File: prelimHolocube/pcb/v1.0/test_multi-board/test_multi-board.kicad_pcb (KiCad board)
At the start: 2 copper layers, 120 x 100 mm, 48 parts

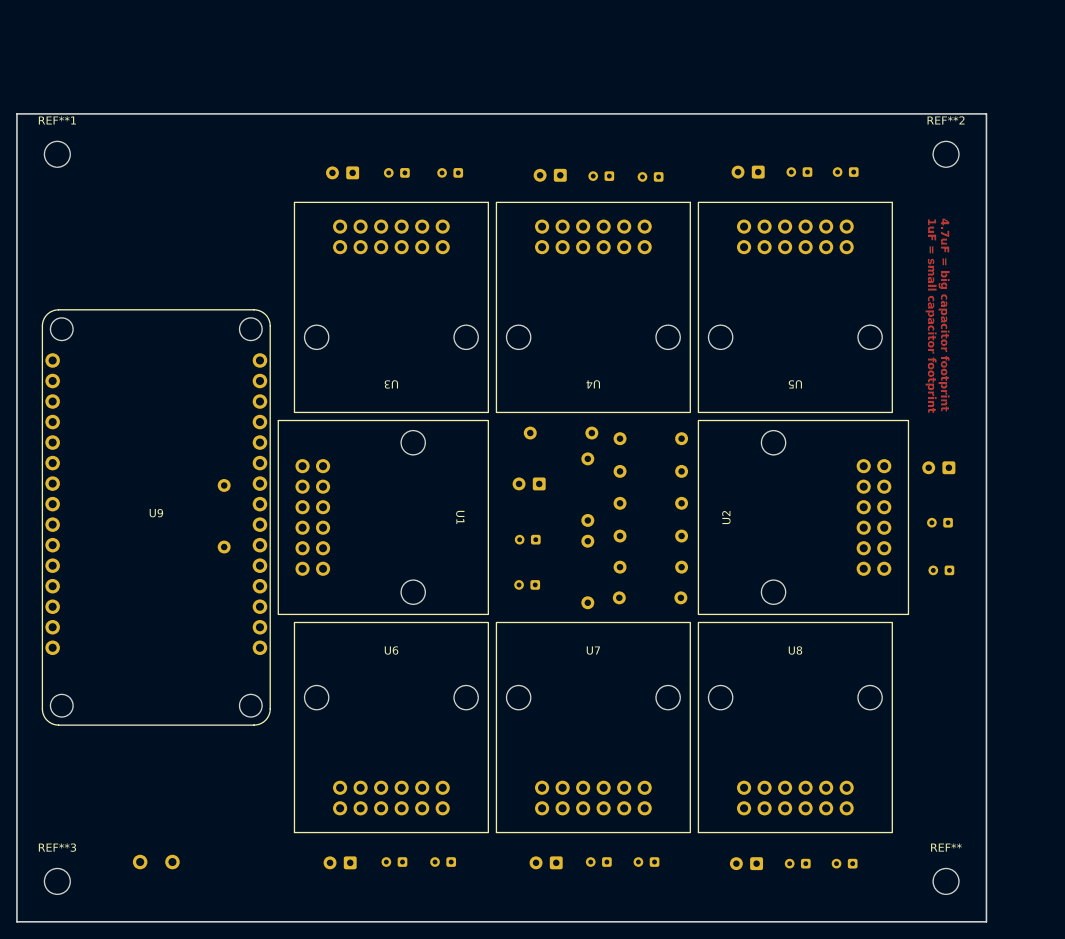
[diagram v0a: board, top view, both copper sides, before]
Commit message: Finish schematic
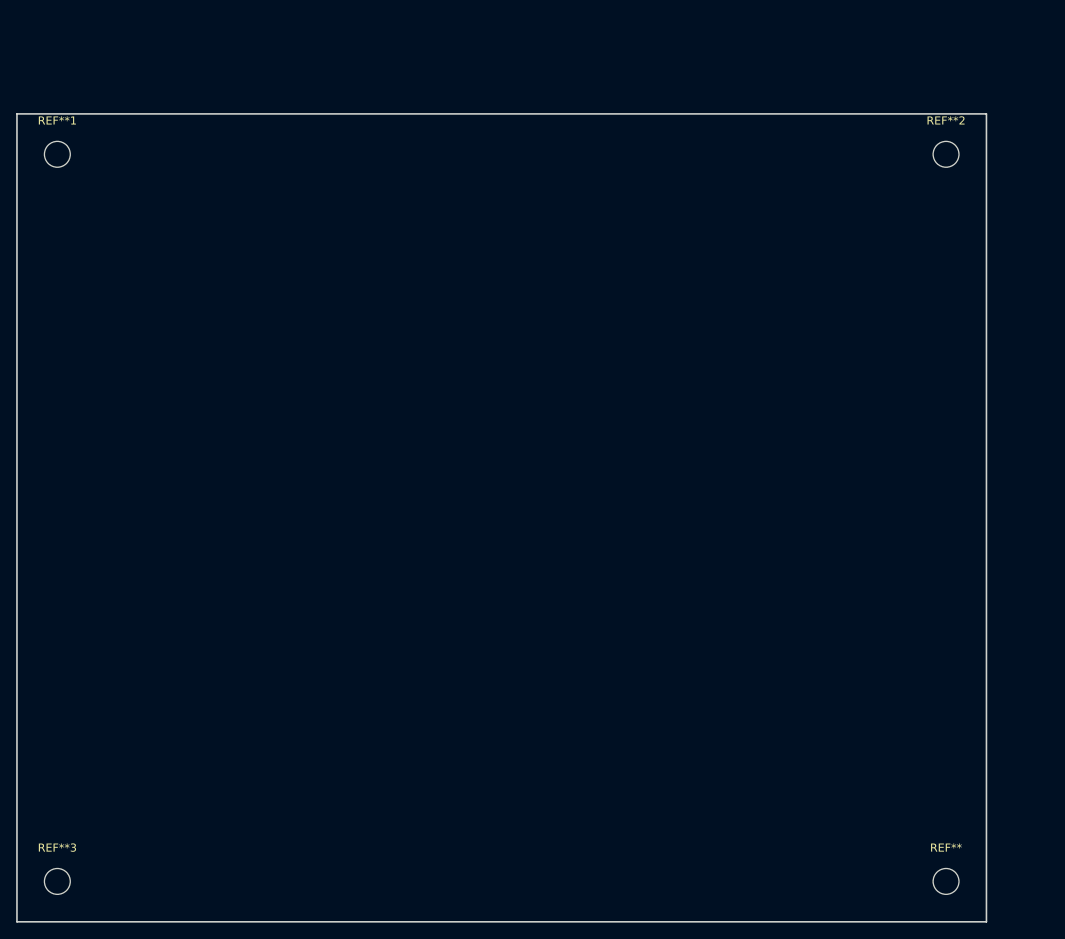
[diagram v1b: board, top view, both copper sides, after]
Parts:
- removed C1, C11, C12, C14, C16, C17, C18, C20, C22, C23, C24, C3, C5, C6, C8, C9: 4.7uF, Capacitor_THT:CP_Radial_D4.0mm_P2.00mm
- removed C10, C13, C15, C19, C2, C21, C4, C7: 1uF ceramic, Capacitor_THT:CP_Radial_D5.0mm_P2.50mm
- removed R1, R10, R2, R4, R5, R6, R7, R8, R9: 1M, Resistor_THT:R_Axial_DIN0207_L6.3mm_D2.5mm_P7.62mm_Horizontal
- removed R3: 10k, Resistor_THT:R_Axial_DIN0207_L6.3mm_D2.5mm_P7.62mm_Horizontal
- removed U1, U2, U3, U4, U5, U6, U7, U8: ~, transparent_oled_display:surenoo-1.12in-128x128
- removed U10: ~, Power_Supply:DC_2-Terminals
- removed U9: ~, esp32:devkitv1-30pin
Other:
- board text removed: "4.7uF = big capacitor footprint 1uF = small capacitor footprint"

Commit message: Finish multiboard pcb
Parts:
- removed REF**: MountingHole_3.2mm_M3, MountingHole:MountingHole_3.2mm_M3
- added C1: 4.7uF, Capacitor_THT:CP_Radial_D4.0mm_P2.00mm, F.Cu at (109.9, 69.6)
- added C10: 4.7uF, Capacitor_THT:CP_Radial_D4.0mm_P2.00mm, F.Cu at (190.6, 69.7)
- added C11: 1uF ceramic, Capacitor_THT:C_Disc_D6.0mm_W2.5mm_P5.00mm, F.Cu at (198.7, 74.5)
- added C12: 4.7uF, Capacitor_THT:CP_Radial_D4.0mm_P2.00mm, F.Cu at (185.3, 69.7)
- added C13: 4.7uF, Capacitor_THT:CP_Radial_D4.0mm_P2.00mm, F.Cu at (119.1, 122.2)
- added C14: 1uF ceramic, Capacitor_THT:C_Disc_D6.0mm_W2.5mm_P5.00mm, F.Cu at (110.8, 117.2)
- added C15: 4.7uF, Capacitor_THT:CP_Radial_D4.0mm_P2.00mm, F.Cu at (124.1, 122.1)
- added C16: 4.7uF, Capacitor_THT:CP_Radial_D4.0mm_P2.00mm, F.Cu at (145.9, 122.1)
- added C17: 1uF ceramic, Capacitor_THT:C_Disc_D6.0mm_W2.5mm_P5.00mm, F.Cu at (137.8, 117.1)
- added C18: 4.7uF, Capacitor_THT:CP_Radial_D4.0mm_P2.00mm, F.Cu at (151.3, 122.0)
- added C19: 4.7uF, Capacitor_THT:CP_Radial_D4.0mm_P2.00mm, F.Cu at (173.2, 121.9)
- added C2: 1uF ceramic, Capacitor_THT:C_Disc_D6.0mm_W2.5mm_P5.00mm, F.Cu at (117.7, 74.5)
- added C20: 1uF ceramic, Capacitor_THT:C_Disc_D6.0mm_W2.5mm_P5.00mm, F.Cu at (165.3, 117.1)
- added C21: 4.7uF, Capacitor_THT:CP_Radial_D4.0mm_P2.00mm, F.Cu at (178.3, 121.9)
- added C22: 4.7uF, Capacitor_THT:CP_Radial_D4.0mm_P2.00mm, F.Cu at (199.5, 121.9)
- added C23: 1uF ceramic, Capacitor_THT:C_Disc_D6.0mm_W2.5mm_P5.00mm, F.Cu at (191.5, 117.1)
- added C24: 4.7uF, Capacitor_THT:CP_Radial_D4.0mm_P2.00mm, F.Cu at (204.8, 121.8)
- added C3: 4.7uF, Capacitor_THT:CP_Radial_D4.0mm_P2.00mm, F.Cu at (104.7, 69.7)
- added C4: 4.7uF, Capacitor_THT:CP_Radial_D4.0mm_P2.00mm, F.Cu at (136.8, 69.6)
- added C5: 1uF ceramic, Capacitor_THT:C_Disc_D6.0mm_W2.5mm_P5.00mm, F.Cu at (144.6, 74.5)
- added C6: 4.7uF, Capacitor_THT:CP_Radial_D4.0mm_P2.00mm, F.Cu at (131.7, 69.6)
- added C7: 4.7uF, Capacitor_THT:CP_Radial_D4.0mm_P2.00mm, F.Cu at (164.0, 69.7)
- added C8: 1uF ceramic, Capacitor_THT:C_Disc_D6.0mm_W2.5mm_P5.00mm, F.Cu at (171.8, 74.6)
- added C9: 4.7uF, Capacitor_THT:CP_Radial_D4.0mm_P2.00mm, F.Cu at (158.7, 69.7)
- added J1: Breakout_1, Connector_PinHeader_2.54mm:PinHeader_1x04_P2.54mm_Vertical, F.Cu at (124.4, 77.8)
- added J2: Breakout_2, Connector_PinHeader_2.54mm:PinHeader_1x04_P2.54mm_Vertical, F.Cu at (151.6, 77.8)
- added J3: Breakout_3, Connector_PinHeader_2.54mm:PinHeader_1x04_P2.54mm_Vertical, F.Cu at (178.7, 77.8)
- added J4: Breakout_4, Connector_PinHeader_2.54mm:PinHeader_1x04_P2.54mm_Vertical, F.Cu at (205.3, 77.8)
- added J5: Breakout_5, Connector_PinHeader_2.54mm:PinHeader_1x04_P2.54mm_Vertical, F.Cu at (104.1, 114.0)
- added J6: Breakout_6, Connector_PinHeader_2.54mm:PinHeader_1x04_P2.54mm_Vertical, F.Cu at (131.1, 113.8)
- added J7: Breakout_7, Connector_PinHeader_2.54mm:PinHeader_1x04_P2.54mm_Vertical, F.Cu at (158.2, 113.7)
- added J8: Breakout_8, Connector_PinHeader_2.54mm:PinHeader_1x04_P2.54mm_Vertical, F.Cu at (184.8, 113.7)
- added R1: 750k, Resistor_THT:R_Axial_DIN0207_L6.3mm_D2.5mm_P7.62mm_Horizontal, F.Cu at (114.2, 77.1)
- added R10: 750k, Resistor_THT:R_Axial_DIN0207_L6.3mm_D2.5mm_P7.62mm_Horizontal, F.Cu at (194.9, 77.1)
- added R11: 10k, Resistor_THT:R_Axial_DIN0207_L6.3mm_D2.5mm_P7.62mm_Horizontal, F.Cu at (151.1, 105.3)
- added R12: 10k, Resistor_THT:R_Axial_DIN0207_L6.3mm_D2.5mm_P7.62mm_Horizontal, F.Cu at (147.8, 105.3)
- added R13: 750k, Resistor_THT:R_Axial_DIN0207_L6.3mm_D2.5mm_P7.62mm_Horizontal, F.Cu at (114.5, 114.6)
- added R14: 10k, Resistor_THT:R_Axial_DIN0207_L6.3mm_D2.5mm_P7.62mm_Horizontal, F.Cu at (162.5, 88.9)
- added R16: 750k, Resistor_THT:R_Axial_DIN0207_L6.3mm_D2.5mm_P7.62mm_Horizontal, F.Cu at (141.4, 114.5)
- added R19: 750k, Resistor_THT:R_Axial_DIN0207_L6.3mm_D2.5mm_P7.62mm_Horizontal, F.Cu at (168.9, 114.5)
- added R2: 10k, Resistor_THT:R_Axial_DIN0207_L6.3mm_D2.5mm_P7.62mm_Horizontal, F.Cu at (157.4, 85.7)
- added R22: 750k, Resistor_THT:R_Axial_DIN0207_L6.3mm_D2.5mm_P7.62mm_Horizontal, F.Cu at (195.2, 114.4)
- added R3: 10k, Resistor_THT:R_Axial_DIN0207_L6.3mm_D2.5mm_P7.62mm_Horizontal, F.Cu at (167.6, 105.3)
- added R4: 750k, Resistor_THT:R_Axial_DIN0207_L6.3mm_D2.5mm_P7.62mm_Horizontal, F.Cu at (141.2, 77.0)
- added R5: 10k, Resistor_THT:R_Axial_DIN0207_L6.3mm_D2.5mm_P7.62mm_Horizontal, F.Cu at (164.3, 105.3)
- added R6: 10k, Resistor_THT:R_Axial_DIN0207_L6.3mm_D2.5mm_P7.62mm_Horizontal, F.Cu at (161.0, 105.3)
- added R7: 750k, Resistor_THT:R_Axial_DIN0207_L6.3mm_D2.5mm_P7.62mm_Horizontal, F.Cu at (168.3, 77.2)
- added R8: 10k, Resistor_THT:R_Axial_DIN0207_L6.3mm_D2.5mm_P7.62mm_Horizontal, F.Cu at (157.7, 105.3)
- added R9: 10k, Resistor_THT:R_Axial_DIN0207_L6.3mm_D2.5mm_P7.62mm_Horizontal, F.Cu at (154.4, 105.3)
- added REF**4: MountingHole_3.2mm_M3, MountingHole:MountingHole_3.2mm_M3, F.Cu at (98.0, 147.6)
- added U1: ~, transparent_oled_display:surenoo-1.12in-128x128, F.Cu at (114.3, 55.1)
- added U10: ~, Connector_PinHeader_2.54mm:PinHeader_1x02_P2.54mm_Vertical, F.Cu at (186.4, 85.9)
- added U2: ~, transparent_oled_display:surenoo-1.12in-128x128, F.Cu at (141.3, 55.0)
- added U3: ~, transparent_oled_display:surenoo-1.12in-128x128, F.Cu at (168.5, 55.0)
- added U4: ~, transparent_oled_display:surenoo-1.12in-128x128, F.Cu at (195.1, 55.0)
- added U5: ~, transparent_oled_display:surenoo-1.12in-128x128, F.Cu at (114.3, 136.8)
- added U6: ~, transparent_oled_display:surenoo-1.12in-128x128, F.Cu at (141.3, 136.8)
- added U7: ~, transparent_oled_display:surenoo-1.12in-128x128, F.Cu at (168.4, 136.7)
- added U8: ~, transparent_oled_display:surenoo-1.12in-128x128, F.Cu at (195.0, 136.7)
- added U9: ~, esp32:devkitv1-30pin, F.Cu at (156.5, 95.5)
- moved REF**3 156.4 mm to (212.6, 44.8)
- moved REF**1 148.7 mm to (212.6, 147.6)
- moved REF**2 107.2 mm to (98.0, 44.8)
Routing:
- net VDD_1: track 0.00 -> 636.2 mm, vias 0 -> 2
- net VPP_1: track 0.00 -> 580.8 mm
- net RES: track 0.00 -> 354.6 mm, vias 0 -> 6
- net SCL: track 0.00 -> 349.6 mm, vias 0 -> 15
- net SI: track 0.00 -> 348.4 mm, vias 0 -> 15
- net A0: track 0.00 -> 334.8 mm, vias 0 -> 19
- net GND: track 0.00 -> 224.8 mm, vias 0 -> 27
- net CS_1: track 0.00 -> 95.2 mm, vias 0 -> 2
- net CS_4: track 0.00 -> 79.2 mm, vias 0 -> 3
- net CS_2: track 0.00 -> 74.2 mm, vias 0 -> 6
- net CS_8: track 0.00 -> 72.0 mm, vias 0 -> 7
- net CS_5: track 0.00 -> 65.2 mm, vias 0 -> 6
- net CS_3: track 0.00 -> 61.6 mm, vias 0 -> 5
- net CS_7: track 0.00 -> 38.6 mm, vias 0 -> 3
- net CS_6: track 0.00 -> 31.7 mm, vias 0 -> 2
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- added copper zone on B.Cu, net GND
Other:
- board size 120 x 100 mm -> 123.6 x 111.8 mm
- board text added: "+"
- board text added: "+3.3V"
- board text added: "-"
- board text added: "10k"
- board text added: "1uF"
- board text added: "4.7uF"
- board text added: "750k"
- board text added: "GND"
- board text added: "HOLOCUBE"
- board text added: "Holocube v1.0 Testing Phase: Multi-Board"
- board text added: "IREF"
- board text added: "M3"
- board text added: "Made with love By Jayden, 17, Boston"
- board text added: "VCOMH"
- board text added: "VDD"
- board text added: "VPP"
